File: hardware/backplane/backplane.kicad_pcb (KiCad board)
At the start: 2 copper layers, 100 x 100 mm, 79 parts, among them J1 Raspberry_Pi_2_3, J10 Screw_Terminal_01x02, J11 Screw_Terminal_01x02, J12 Conn_02x08_Odd_Even, J2 Conn_02x08_Top_Bottom, J3 RJ45, J4 RJ45, J5 RJ45, J6 RJ45, J7 Screw_Terminal_01x03, J8 Conn_01x03, J9 Conn_02x08_Odd_Even, Q1 Q_NMOS_GSD, Q2 Q_NMOS_GSD, Q3 ZXMP4A16G, Q4 ZXMP4A16G, Q5 ZXMP4A16G, U1 MCP23017_SO, U2 MCP2515-xSO, U3 TJA1051T/3, U4 PAM8403, Y1 8MHz

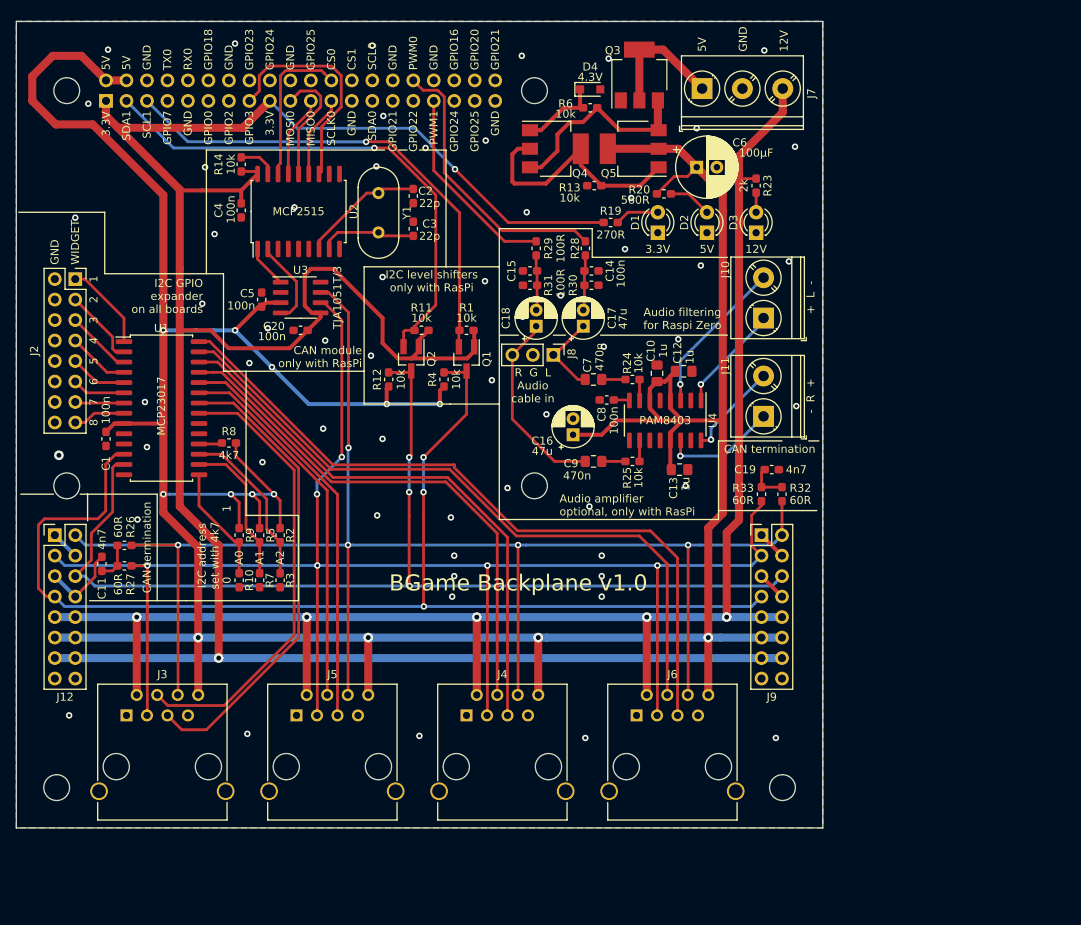
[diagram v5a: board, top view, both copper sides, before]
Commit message: Backplane PCB: some rerouting to avoid vias in I2C/CAN
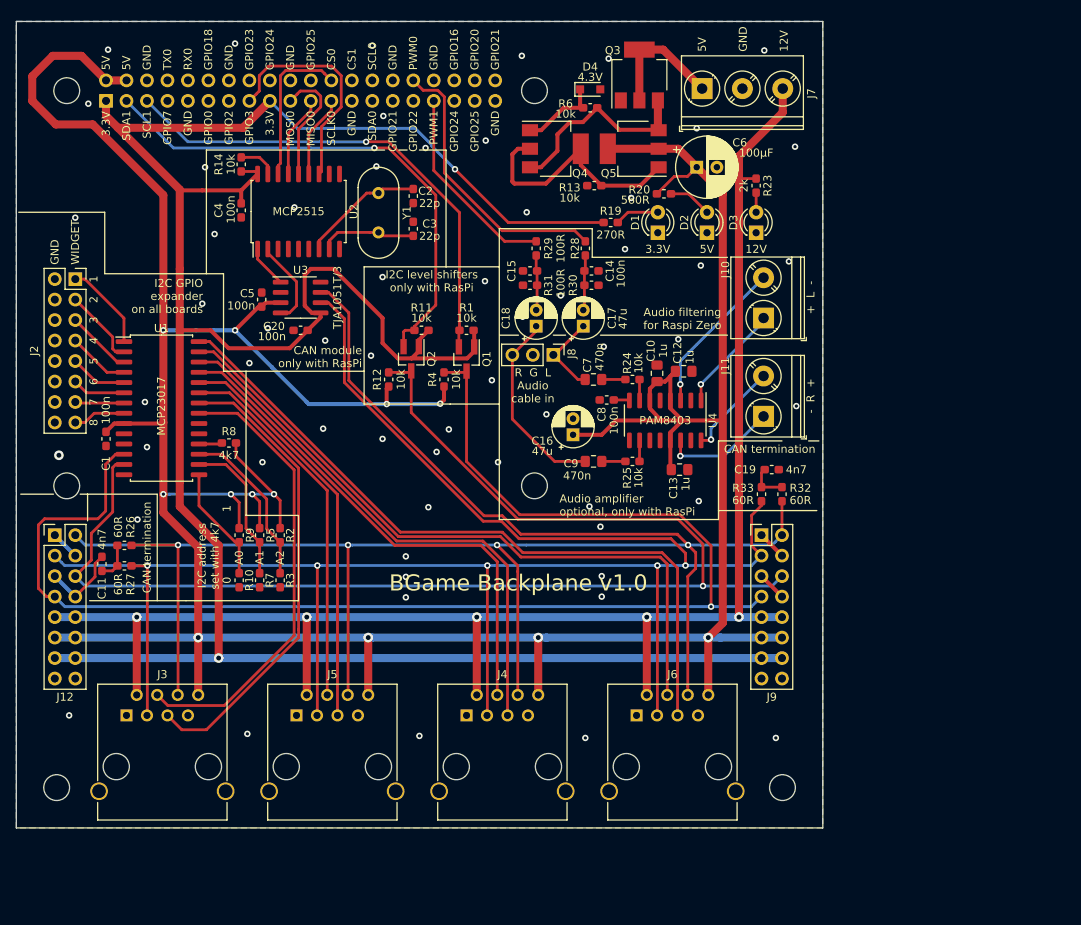
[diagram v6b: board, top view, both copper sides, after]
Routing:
- net CAN_H: track 206.5 -> 238.4 mm, vias 5 -> 4
- net CAN_L: track 208.0 -> 237.1 mm, vias 6 -> 5
- net SDA: track 135.3 -> 161.8 mm, vias 3 -> 1
- net SCL: track 150.9 -> 172.9 mm, vias 3 -> 1
- net MODULE_READY_2: track 65.3 -> 63.2 mm
- net MODULE_ENABLE_2: track 69.3 -> 67.3 mm
- net MODULE_ENABLE_3: track 90.2 -> 89.2 mm
- net +12V: track 199.3 -> 198.7 mm
- net VCC: vias 13 -> 12
- net GND: vias 59 -> 60

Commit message: Backplane PCB: remove 3.3V from backplane connector
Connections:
- J12 pad 13: +3V3 -> Net-(J12-Pad13)
- J12 pad 14: +3V3 -> Net-(J12-Pad14)
- J9 pad 13: +3V3 -> Net-(J9-Pad13)
- J9 pad 14: +3V3 -> Net-(J9-Pad14)
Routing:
- net +3V3: track 309.0 -> 172.4 mm, vias 2 -> 1
- net GND: vias 60 -> 67
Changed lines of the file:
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@@
     (thickness 1.6)
     (drawings 172)
-    (tracks 633)
+    (tracks 627)
     (zones 0)
     (modules 79)
-    (nets 96)
+    (nets 100)
   )
   (page A4)
@@
   )
   (setup
-    (last_trace_width 0.35)
+    (last_trace_width 0.5)
     (user_trace_width 0.35)
     (user_trace_width 0.5)
@@
   (net 94 "Net-(D4-Pad1)")
   (net 95 +5V)
+  (net 96 "Net-(J9-Pad14)")
+  (net 97 "Net-(J9-Pad13)")
+  (net 98 "Net-(J12-Pad14)")
+  (net 99 "Net-(J12-Pad13)")
   (net_class Default "This is the default net class."
     (clearance 0.2)
@@
     (add_net "Net-(J1-Pad7)")
     (add_net "Net-(J1-Pad8)")
+    (add_net "Net-(J12-Pad13)")
+    (add_net "Net-(J12-Pad14)")
     (add_net "Net-(J2-Pad1)")
     (add_net "Net-(J2-Pad11)")
@@
     (add_net "Net-(J2-Pad7)")
     (add_net "Net-(J2-Pad9)")
+    (add_net "Net-(J9-Pad13)")
+    (add_net "Net-(J9-Pad14)")
     (add_net "Net-(Q3-Pad3)")
     (add_net "Net-(Q4-Pad2)")
@@
       (net 1 GND))
     (pad 14 thru_hole oval (at 2.54 15.24) (size 1.7 1.7) (drill 1) (layers *.Cu *.Mask)
-      (net 2 +3V3))
+      (net 98 "Net-(J12-Pad14)"))
     (pad 13 thru_hole oval (at 0 15.24) (size 1.7 1.7) (drill 1) (layers *.Cu *.Mask)
-      (net 2 +3V3))
+      (net 99 "Net-(J12-Pad13)"))
     (pad 12 thru_hole oval (at 2.54 12.7) (size 1.7 1.7) (drill 1) (layers *.Cu *.Mask)
       (net 3 VCC))
@@
       (net 1 GND))
     (pad 14 thru_hole oval (at 2.54 15.24) (size 1.7 1.7) (drill 1) (layers *.Cu *.Mask)
-      (net 2 +3V3))
+      (net 96 "Net-(J9-Pad14)"))
     (pad 13 thru_hole oval (at 0 15.24) (size 1.7 1.7) (drill 1) (layers *.Cu *.Mask)
-      (net 2 +3V3))
+      (net 97 "Net-(J9-Pad13)"))
     (pad 12 thru_hole oval (at 2.54 12.7) (size 1.7 1.7) (drill 1) (layers *.Cu *.Mask)
       (net 3 VCC))
@@
   (via (at 144.178 138.844) (size 0.8) (drill 0.4) (layers F.Cu B.Cu) (net 1))
   (via (at 121.064 110.142) (size 0.8) (drill 0.4) (layers F.Cu B.Cu) (net 1))
-  (via (at 73.058 84.996) (size 0.8) (drill 0.4) (layers F.Cu B.Cu) (net 1))
   (via (at 84.488 73.058) (size 0.8) (drill 0.4) (layers F.Cu B.Cu) (net 1))
   (via (at 95.41 81.694) (size 0.8) (drill 0.4) (layers F.Cu B.Cu) (net 1))
@@
   (via (at 101.092 110.236) (size 0.8) (drill 0.4) (layers F.Cu B.Cu) (net 1))
   (via (at 122.428 112.649) (size 0.8) (drill 0.4) (layers F.Cu B.Cu) (net 1))
-  (segment (start 142.4 128.938) (end 144.94 128.938) (width 1) (layer B.Cu) (net 2))
-  (segment (start 54.77 128.938) (end 57.31 128.938) (width 1) (layer B.Cu) (net 2))
-  (segment (start 75.09 128.938) (end 142.4 128.938) (width 1) (layer B.Cu) (net 2))
-  (segment (start 57.31 128.938) (end 75.09 128.938) (width 1) (layer B.Cu) (net 2))
+  (via (at 70.358 86.487) (size 0.8) (drill 0.4) (layers F.Cu B.Cu) (net 1))
+  (via (at 75.184 116.078) (size 0.8) (drill 0.4) (layers F.Cu B.Cu) (net 1))
+  (via (at 75.184 118.618) (size 0.8) (drill 0.4) (layers F.Cu B.Cu) (net 1))
+  (via (at 75.184 121.158) (size 0.8) (drill 0.4) (layers F.Cu B.Cu) (net 1))
+  (via (at 74.422 113.538) (size 0.8) (drill 0.4) (layers F.Cu B.Cu) (net 1))
+  (via (at 70.358 103.124) (size 0.8) (drill 0.4) (layers F.Cu B.Cu) (net 1))
+  (via (at 75.692 84.836) (size 0.8) (drill 0.4) (layers F.Cu B.Cu) (net 1))
+  (via (at 64.516 82.55) (size 0.8) (drill 0.4) (layers F.Cu B.Cu) (net 1))
   (segment (start 61.12 61.7) (end 61.12 59.85) (width 1) (layer F.Cu) (net 2))
-  (segment (start 75.09 128.938) (end 75.09 114.968) (width 1) (layer F.Cu) (net 2))
-  (segment (start 75.09 114.968) (end 70.264 110.142) (width 1) (layer F.Cu) (net 2))
   (segment (start 77.884 70.948) (end 79.916 68.916) (width 0.5) (layer F.Cu) (net 2))
   (segment (start 77.884 72.55) (end 77.884 70.948) (width 0.5) (layer F.Cu) (net 2))
-  (segment (start 70.368 70.948) (end 70.264 70.844) (width 0.5) (layer F.Cu) (net 2))
-  (segment (start 73.058 70.948) (end 70.368 70.948) (width 0.5) (layer F.Cu) (net 2))
   (segment (start 62.608 63.188) (end 61.12 61.7) (width 1) (layer F.Cu) (net 2))
-  (segment (start 70.264 70.844) (end 62.608 63.188) (width 1) (layer F.Cu) (net 2))
   (segment (start 79.599 68.599) (end 79.916 68.916) (width 0.35) (layer F.Cu) (net 2))
   (segment (start 77.884 68.599) (end 79.599 68.599) (width 0.35) (layer F.Cu) (net 2))
-  (segment (start 70.264 80.678) (end 70.264 70.844) (width 1) (layer F.Cu) (net 2))
-  (segment (start 70.264 83.98) (end 70.264 80.678) (width 1) (layer F.Cu) (net 2))
   (segment (start 78.102 63.188) (end 81.44 59.85) (width 1) (layer F.Cu) (net 2))
   (segment (start 62.608 63.188) (end 78.102 63.188) (width 1) (layer F.Cu) (net 2))
@@
   (segment (start 106.774 88.373) (end 106.699 88.298) (width 0.5) (layer F.Cu) (net 2))
   (segment (start 106.774 90.354) (end 106.774 88.373) (width 0.5) (layer F.Cu) (net 2))
-  (segment (start 73.058 70.948) (end 77.884 70.948) (width 0.5) (layer F.Cu) (net 2))
   (segment (start 87.725 86.698) (end 86.125 88.298) (width 0.5) (layer F.Cu) (net 2))
   (segment (start 87.725 86.139) (end 87.725 86.698) (width 0.5) (layer F.Cu) (net 2))
-  (segment (start 70.264 107.094) (end 70.264 88.298) (width 1) (layer F.Cu) (net 2))
-  (segment (start 70.264 88.298) (end 70.264 83.98) (width 1) (layer F.Cu) (net 2))
-  (segment (start 70.264 88.298) (end 74.100035 88.298) (width 0.5) (layer F.Cu) (net 2))
-  (segment (start 83.900989 90.522011) (end 86.125 88.298) (width 0.5) (layer F.Cu) (net 2))
-  (segment (start 74.100035 88.298) (end 76.324046 90.522011) (width 0.5) (layer F.Cu) (net 2))
-  (segment (start 76.324046 90.522011) (end 83.900989 90.522011) (width 0.5) (layer F.Cu) (net 2))
   (segment (start 87.725 86.139) (end 86.647 86.139) (width 0.5) (layer F.Cu) (net 2))
   (segment (start 86.647 86.139) (end 85.758 85.25) (width 0.5) (layer F.Cu) (net 2))
@@
   (segment (start 97.305998 91.78) (end 99.016 91.78) (width 0.5) (layer F.Cu) (net 2))
   (segment (start 95.41 86.774) (end 95.41 89.884002) (width 0.5) (layer F.Cu) (net 2))
-  (segment (start 70.264 110.142) (end 70.264 107.094) (width 1) (layer F.Cu) (net 2))
-  (via (at 75.09 128.938) (size 1.2) (drill 0.6) (layers F.Cu B.Cu) (net 2))
   (segment (start 81.44 59.85) (end 84.836 63.246) (width 0.35) (layer B.Cu) (net 2))
   (via (at 104.394 68.326) (size 0.8) (drill 0.4) (layers F.Cu B.Cu) (net 2))
@@
   (segment (start 110.998 74.93) (end 104.394 68.326) (width 0.35) (layer F.Cu) (net 2))
   (segment (start 110.998 74.93) (end 122.823 74.93) (width 0.35) (layer F.Cu) (net 2))
+  (segment (start 73.058 70.948) (end 77.884 70.948) (width 0.5) (layer F.Cu) (net 2))
+  (segment (start 73.058 70.948) (end 70.368 70.948) (width 0.5) (layer F.Cu) (net 2))
+  (segment (start 62.608 63.188) (end 70.368 70.948) (width 0.5) (layer F.Cu) (net 2))
+  (segment (start 70.368 83.564002) (end 70.358 83.574002) (width 0.5) (layer F.Cu) (net 2))
+  (segment (start 70.368 70.948) (end 70.368 83.564002) (width 0.5) (layer F.Cu) (net 2))
+  (segment (start 76.324046 89.520048) (end 70.368 83.564002) (width 0.5) (layer F.Cu) (net 2))
+  (segment (start 84.902952 89.520048) (end 86.125 88.298) (width 0.5) (layer F.Cu) (net 2))
+  (segment (start 76.324046 89.520048) (end 84.902952 89.520048) (width 0.5) (layer F.Cu) (net 2))
   (segment (start 142.4 126.398) (end 144.94 126.398) (width 1) (layer B.Cu) (net 3))
   (segment (start 54.77 126.398) (end 57.31 126.398) (width 1) (layer B.Cu) (net 3))
@@
   (segment (start 77.63 109.634) (end 76.614 108.618) (width 0.35) (layer F.Cu) (net 3))
   (segment (start 77.63 112.823) (end 77.63 109.634) (width 0.35) (layer F.Cu) (net 3))
-  (segment (start 72.55 115.222) (end 72.55 126.398) (width 1) (layer F.Cu) (net 3))
-  (segment (start 68.232 110.904) (end 72.55 115.222) (width 1) (layer F.Cu) (net 3))
   (via (at 68.232 108.618) (size 0.8) (drill 0.4) (layers F.Cu B.Cu) (net 3))
   (segment (start 68.232 99.728) (end 68.232 108.618) (width 1) (layer F.Cu) (net 3))
   (segment (start 68.994 108.618) (end 68.232 108.618) (width 0.35) (layer B.Cu) (net 3))
-  (segment (start 68.232 108.618) (end 68.232 110.904) (width 1) (layer F.Cu) (net 3))
   (segment (start 72.55 133.51) (end 72.55 126.398) (width 1) (layer F.Cu) (net 3))
   (via (at 114.714 126.398) (size 1.2) (drill 0.6) (layers F.Cu B.Cu) (net 3))
@@
   (segment (start 103.03 95.269) (end 103.03 96.934) (width 0.5) (layer F.Cu) (net 3))
   (segment (start 103.03 96.934) (end 102.562015 97.401985) (width 0.5) (layer F.Cu) (net 3))
+  (segment (start 72.55 112.936) (end 72.55 126.398) (width 1) (layer F.Cu) (net 3))
+  (segment (start 68.232 108.618) (end 72.55 112.936) (width 1) (layer F.Cu) (net 3))
   (segment (start 119.634 94.394) (end 116.586 91.346) (width 0.35) (layer F.Cu) (net 4))
   (segment (start 120.538 94.394) (end 119.634 94.394) (width 0.35) (layer F.Cu) (net 4))

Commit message: Backplane PCB: thermal pads for power FETs, lots of finishing touches
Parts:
- C1, C11, C14, C15, C19, C2, C20, C3, C4, C5, C8: footprint Capacitor_SMD:C_0603_1608Metric_Pad1.05x0.95mm_HandSolder -> Capacitor_SMD:C_0805_2012Metric_Pad1.15x1.40mm_HandSolder
- moved Q4 4.34 mm to (112.8, 67.3)
- moved Q5 2.75 mm to (124.2, 67.3)
- moved R13 2.75 mm to (119.4, 71.9)
- moved R11 1.30 mm to (98.9, 88.3)
- moved C19 1.02 mm to (143.7, 106.6)
- moved R32 1.02 mm to (144.9, 109.6)
- moved R33 1.02 mm to (142.4, 109.6)
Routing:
- net +5V: track 16.1 -> 0.00 mm, vias 0 -> 8
- net VCC: track 426.8 -> 414.8 mm, vias 12 -> 21
- net Net-(Q3-Pad3): track 25.1 -> 31.2 mm
- net Net-(D4-Pad1): track 10.2 -> 14.9 mm
- net GND: track 20.7 -> 24.8 mm, vias 67 -> 72
- net CAN_L: track 237.1 -> 236.1 mm
- net CAN_H: track 238.4 -> 237.4 mm
- net SDA_3V3: track 64.3 -> 63.7 mm
- added copper zone on B.Cu, net +5V
- added copper zone on F.Cu, net +5V
- added copper zone on B.Cu, net VCC
- added copper zone on F.Cu, net VCC
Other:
- board text added: "100u"
- board text added: "Backplane expansion"
- board text added: "Power input"
- board text added: "Power protection"
- board text added: "Widget connector"
- board text removed: "100µF"
